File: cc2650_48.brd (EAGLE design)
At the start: 51 x 23.1 mm, 21 parts, among them IC1 CC2650F128RGZT, SW1 SPST_TACT-KMR2, SW2 SPST_TACT-KMR2, U402 TPS62233DRY, X3 microUSB

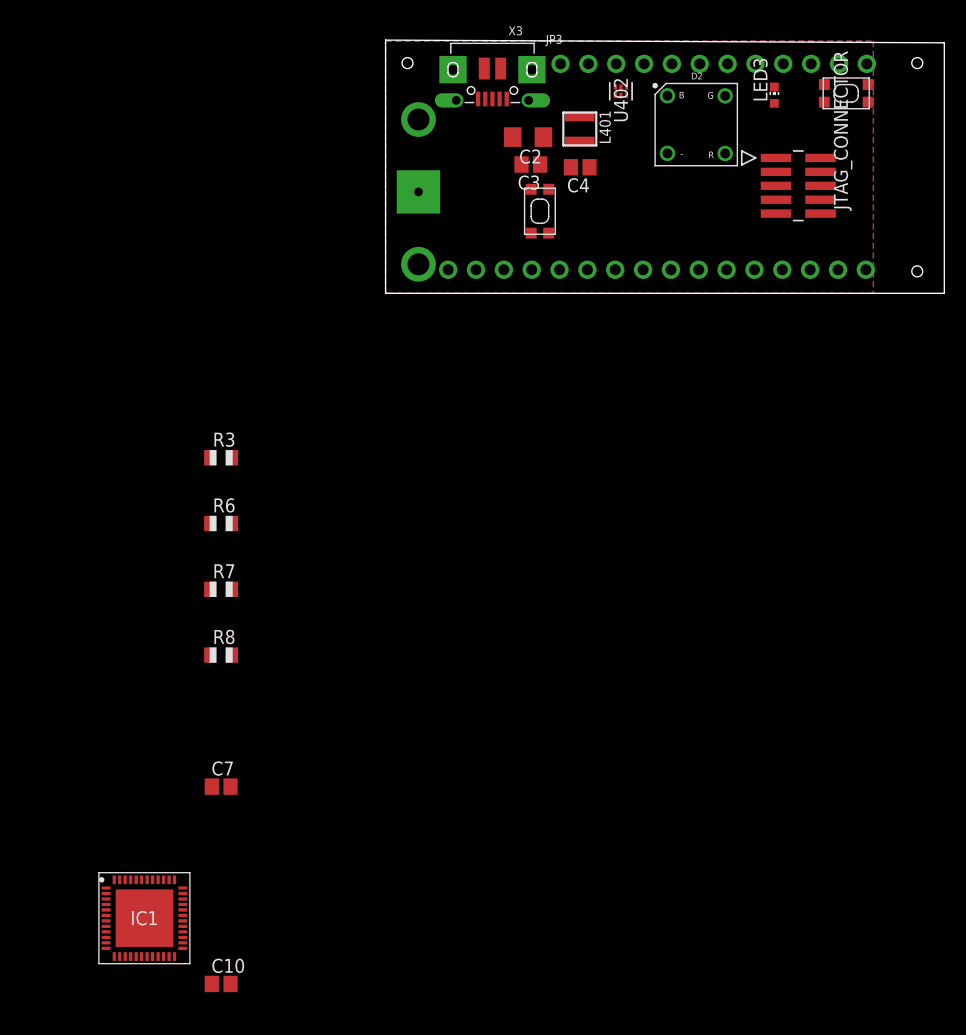
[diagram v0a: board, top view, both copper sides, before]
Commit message: added 48 pin cc2650. change res, cap, led to bigger packages. moved battery to bottom of board. changed micro usb.
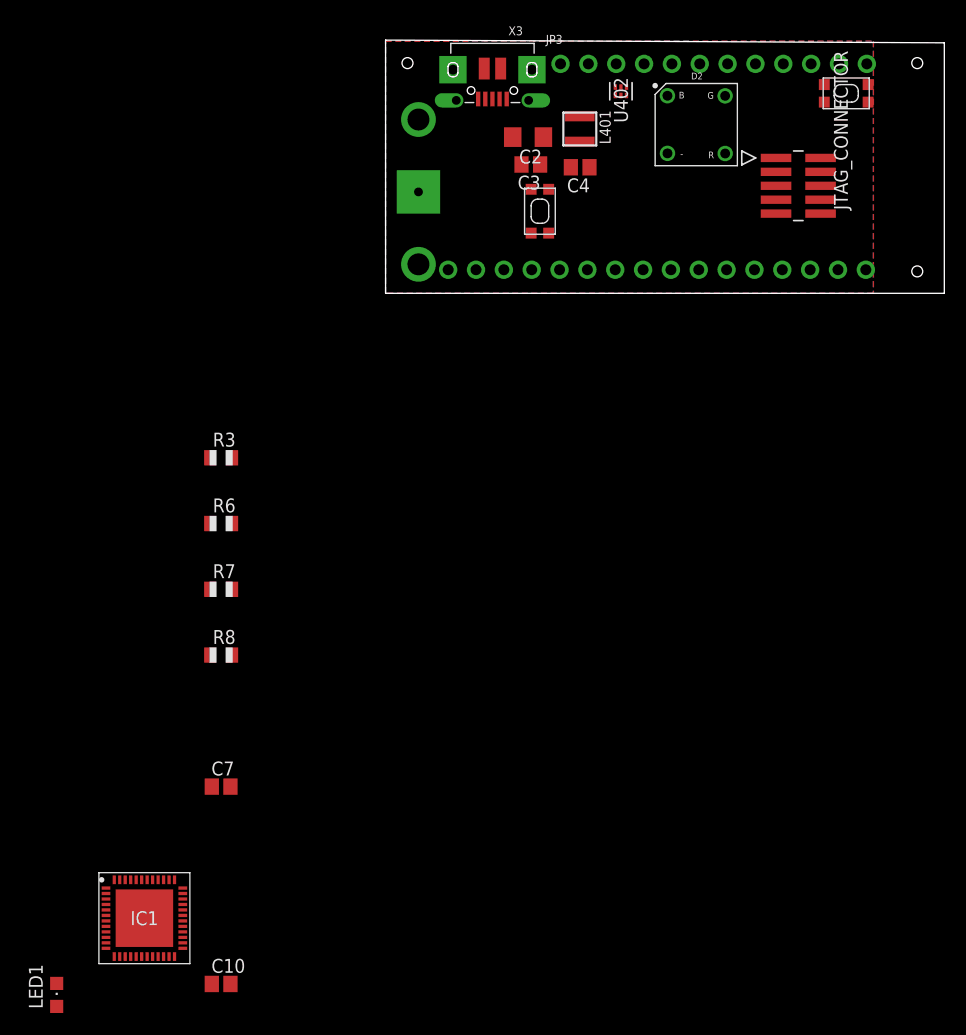
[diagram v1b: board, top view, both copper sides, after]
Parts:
- removed LED3: (no value), led:CHIP-LED0603
- added LED1: (no value), led:CHIPLED_0805
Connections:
- net GND: now also LED1.C; no longer LED3.C
- net N$32: now also LED1.A; no longer LED3.A
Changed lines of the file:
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@@
 <attribute name="OC_NEWARK" value="unknown" x="42.02" y="18.24" size="1.778" layer="27" rot="R180" display="off"/>
-</element>
-<element name="LED3" library="led" library_urn="urn:adsk.eagle:library:259" package="CHIP-LED0603" package3d_urn="urn:adsk.eagle:package:15819/1" value="" x="35.47" y="18.08">
-<attribute name="MF" value="" x="35.47" y="18.08" size="1.778" layer="27" display="off"/>
-<attribute name="MPN" value="HSME-C191" x="35.47" y="18.08" size="1.778" layer="27" display="off"/>
-<attribute name="OC_NEWARK" value="05M0345" x="35.47" y="18.08" size="1.778" layer="27" display="off"/>
 </element>
 <element name="U402" library="tps62231dry" package="DRY6" value="TPS62233DRY" x="21.47" y="18.43" rot="R90">
@@
 <attribute name="SUPPLIER_NAME" value="RS" x="-22" y="-57" size="1.778" layer="27" display="off"/>
 </element>
+<element name="LED1" library="led" library_urn="urn:adsk.eagle:library:259" package="CHIPLED_0805" package3d_urn="urn:adsk.eagle:package:15821/1" value="" x="-30" y="-64"/>
 </elements>
 <signals>
@@
 <contactref element="JTAG_CONNECTOR" pad="3"/>
 <contactref element="JTAG_CONNECTOR" pad="5"/>
-<contactref element="LED3" pad="C"/>
 <contactref element="U402" pad="4"/>
 <contactref element="U402" pad="1"/>
@@
 <contactref element="C7" pad="2"/>
 <contactref element="C10" pad="2"/>
+<contactref element="LED1" pad="C"/>
+<wire x1="-14.15" y1="-63" x2="-30" y2="-62.95" width="0" layer="19" extent="1-1"/>
 <wire x1="-14.15" y1="-45" x2="-14.15" y2="-63" width="0" layer="19" extent="1-1"/>
 <wire x1="-14" y1="-33" x2="-14.15" y2="-45" width="0" layer="19" extent="1-1"/>
 <wire x1="13.33" y1="2.15" x2="-14" y2="-33" width="0" layer="19" extent="1-1"/>
+<wire x1="15.87" y1="2.15" x2="13.33" y2="2.15" width="0" layer="19" extent="1-1"/>
+<wire x1="13.28" y1="5.49" x2="13.33" y2="2.15" width="0" layer="19" extent="1-1"/>
+<wire x1="13.28" y1="9.49" x2="13.28" y2="5.49" width="0" layer="19" extent="1-1"/>
+<wire x1="12.4" y1="11.75" x2="13.28" y2="9.49" width="0" layer="19" extent="1-1"/>
+<wire x1="11.6" y1="14.25" x2="12.4" y2="11.75" width="0" layer="19" extent="1-1"/>
+<wire x1="13.05" y1="17.6" x2="11.6" y2="14.25" width="0" layer="19" extent="1-1"/>
 <wire x1="13.35" y1="20.4" x2="13.05" y2="17.6" width="0" layer="19" extent="1-1"/>
+<wire x1="10.5" y1="20.5" x2="13.35" y2="20.4" width="0" layer="19" extent="1-1"/>
+<wire x1="9" y1="20.5" x2="10.5" y2="20.5" width="0" layer="19" extent="1-1"/>
+<wire x1="8.45" y1="17.725" x2="9" y2="20.5" width="0" layer="19" extent="1-1"/>
+<wire x1="6.45" y1="17.6" x2="8.45" y2="17.725" width="0" layer="19" extent="1-1"/>
 <wire x1="6.15" y1="20.4" x2="6.45" y2="17.6" width="0" layer="19" extent="1-1"/>
-<wire x1="9" y1="20.5" x2="8.45" y2="17.725" width="0" layer="19" extent="1-1"/>
+<wire x1="16.9" y1="11.5" x2="13.28" y2="9.49" width="0" layer="19" extent="1-1"/>
+<wire x1="20.962" y1="18.0744" x2="16.9" y2="11.5" width="0" layer="19" extent="1-1"/>
+<wire x1="21.978" y1="18.811" x2="20.962" y2="18.0744" width="0" layer="19" extent="1-1"/>
+<wire x1="3" y1="9.25" x2="6.45" y2="17.6" width="0" layer="19" extent="1-1"/>
+<wire x1="35.618" y1="11.08" x2="21.978" y2="18.811" width="0" layer="19" extent="1-1"/>
+<wire x1="35.618" y1="9.81" x2="35.618" y2="11.08" width="0" layer="19" extent="1-1"/>
+<wire x1="35.618" y1="7.27" x2="35.618" y2="9.81" width="0" layer="19" extent="1-1"/>
+<wire x1="40.02" y1="17.44" x2="35.618" y2="11.08" width="0" layer="19" extent="1-1"/>
+<wire x1="44.02" y1="17.44" x2="40.02" y2="17.44" width="0" layer="19" extent="1-1"/>
+<wire x1="43.81" y1="2.15" x2="35.618" y2="7.27" width="0" layer="19" extent="1-1"/>
 </signal>
 <signal name="NRESET">
@@
 </signal>
 <signal name="N$32">
-<contactref element="LED3" pad="A"/>
 <contactref element="R6" pad="2"/>
-<wire x1="-14" y1="-21" x2="35.47" y2="17.33" width="0" layer="19" extent="1-1"/>
+<contactref element="LED1" pad="A"/>
+<wire x1="-14" y1="-21" x2="-30" y2="-65.05" width="0" layer="19" extent="1-1"/>
 </signal>
 <signal name="N$14">
